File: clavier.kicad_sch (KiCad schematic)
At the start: 0 parts

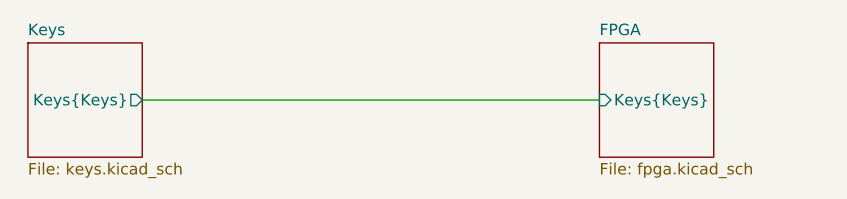
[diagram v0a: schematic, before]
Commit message: Add all keys
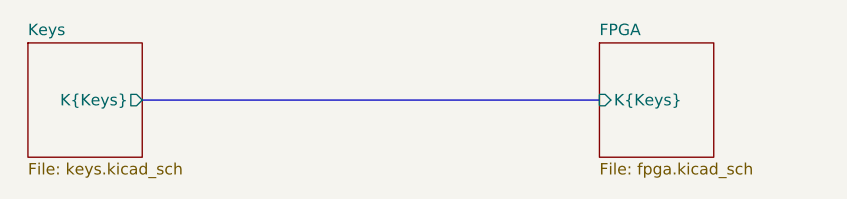
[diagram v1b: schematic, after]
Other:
- sheet FPGA ports: added K{Keys}; removed Keys{Keys}
- sheet Keys ports: added K{Keys}; removed Keys{Keys}
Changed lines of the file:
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@@
 	(generator_version "9.0")
 	(paper "A4")
-	(wire
+	(bus
 		(pts
 			(xy 114.3 82.55) (xy 165.1 82.55)
@@
 			)
 		)
-		(pin "Keys{Keys}" input
+		(pin "K{Keys}" input
 			(at 165.1 82.55 180)
 			(effects
@@
 			)
 		)
-		(pin "Keys{Keys}" output
+		(pin "K{Keys}" output
 			(at 114.3 82.55 0)
 			(effects

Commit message: Initial commit of the PCB
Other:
- sheet FPGA ports: added Kp{KpKeys}; removed none
- sheet Keys ports: added Kp{KpKeys}; removed none
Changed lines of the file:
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@@
 	(bus
 		(pts
-			(xy 114.3 82.55) (xy 165.1 82.55)
+			(xy 127 80.01) (xy 165.1 80.01)
+		)
+		(stroke
+			(width 0)
+			(type default)
+		)
+	)
+	(bus
+		(pts
+			(xy 127 85.09) (xy 165.1 85.09)
 		)
 		(stroke
@@
 	(sheet
 		(at 165.1 76.2)
-		(size 12.7 12.7)
+		(size 25.4 12.7)
 		(exclude_from_sim no)
 		(in_bom yes)
@@
 		)
 		(pin "K{Keys}" input
-			(at 165.1 82.55 180)
+			(at 165.1 80.01 180)
+			(effects
+				(font
+					(size 1.27 1.27)
+				)
+				(justify left)
+			)
+		)
+		(pin "Kp{KpKeys}" input
+			(at 165.1 85.09 180)
 			(effects
 				(font
@@
 	(sheet
 		(at 101.6 76.2)
-		(size 12.7 12.7)
+		(size 25.4 12.7)
 		(exclude_from_sim no)
 		(in_bom yes)
@@
 			)
 		)
-		(pin "K{Keys}" output
-			(at 114.3 82.55 0)
+		(pin "Kp{KpKeys}" output
+			(at 127 85.09 0)
 			(effects
 				(font
+					(size 1.27 1.27)
+				)
+				(justify right)
+			)
+		)
+		(pin "K{Keys}" output
+			(at 127 80.01 0)
+			(effects
+				(font
